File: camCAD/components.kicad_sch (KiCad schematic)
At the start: 12 parts, among them J4 ILI9341_Display_Header, U4 AP3602AKTR-G1 Charge Pump, U5 Flash LED, U6 ADA 254

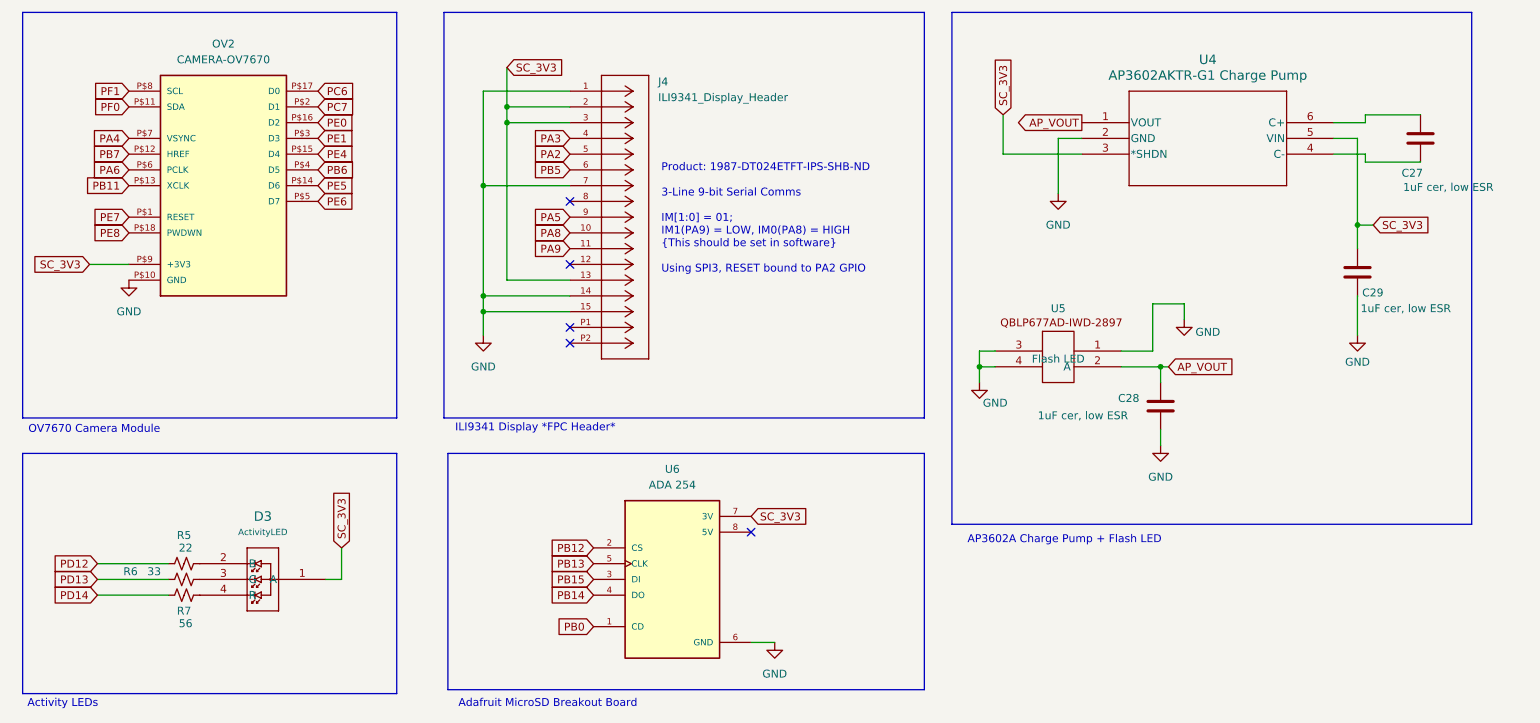
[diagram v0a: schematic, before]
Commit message: REMADE with a much more suitable display
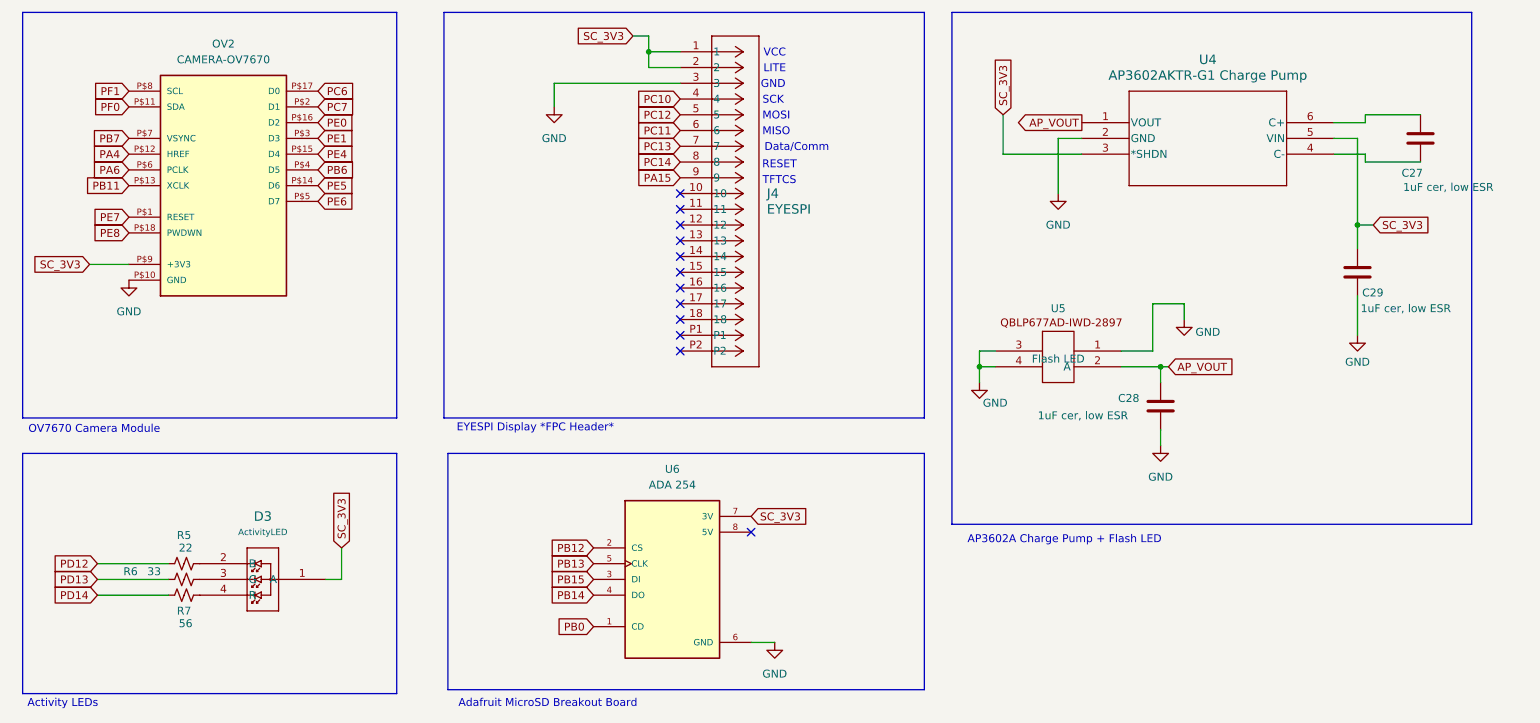
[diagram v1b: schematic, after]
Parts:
- removed J4: ILI9341_Display_Header, 1_Headers:CON_5051101592_MOL, symbol 1_Headers:5051101592
- added J4: EYESPI, CON_5051101892_MOL, symbol 1_Headers:5051101892
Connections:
- net GND: now also J4.3
- net PA4: now also OV2.P$12 (HREF); no longer OV2.P$7 (VSYNC)
- net PB7: now also OV2.P$7 (VSYNC); no longer OV2.P$12 (HREF)
- net SC_3V3: now also J4.1, J4.2
- new net PA15: J4.9
- new net PC10: J4.4
- new net PC11: J4.6
- new net PC12: J4.5
- new net PC13: J4.7
- new net PC14: J4.8
- no-connect marks 5 -> 12
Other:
- note added: "Data/Comm"
- note added: "EYESPI Display *FPC Header*"
- note added: "GND"
- note added: "LITE"
- note added: "MISO"
- note added: "MOSI"
- note added: "RESET"
- note added: "SCK"
- note added: "TFTCS"
- note added: "VCC"
- note removed: "ILI9341 Display *FPC Header*"
- note removed: "Product: 1987-DT024ETFT-IPS-SHB-ND 3-Line 9-bit Serial Comms IM[1:0] = 01; IM1(PA9) = LOW, IM0(PA8) = HIGH {This should be set in software} Using SPI3, RESET bound to PA2 GPIO"
